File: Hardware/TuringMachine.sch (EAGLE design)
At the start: 83 parts, among them IC1 TL072P, IC2 4015, IC3 4015, IC5 4016, IC6 TL072P, IC7 TL072P, T1 2N3904, T2 2N3904, T3 2N3904

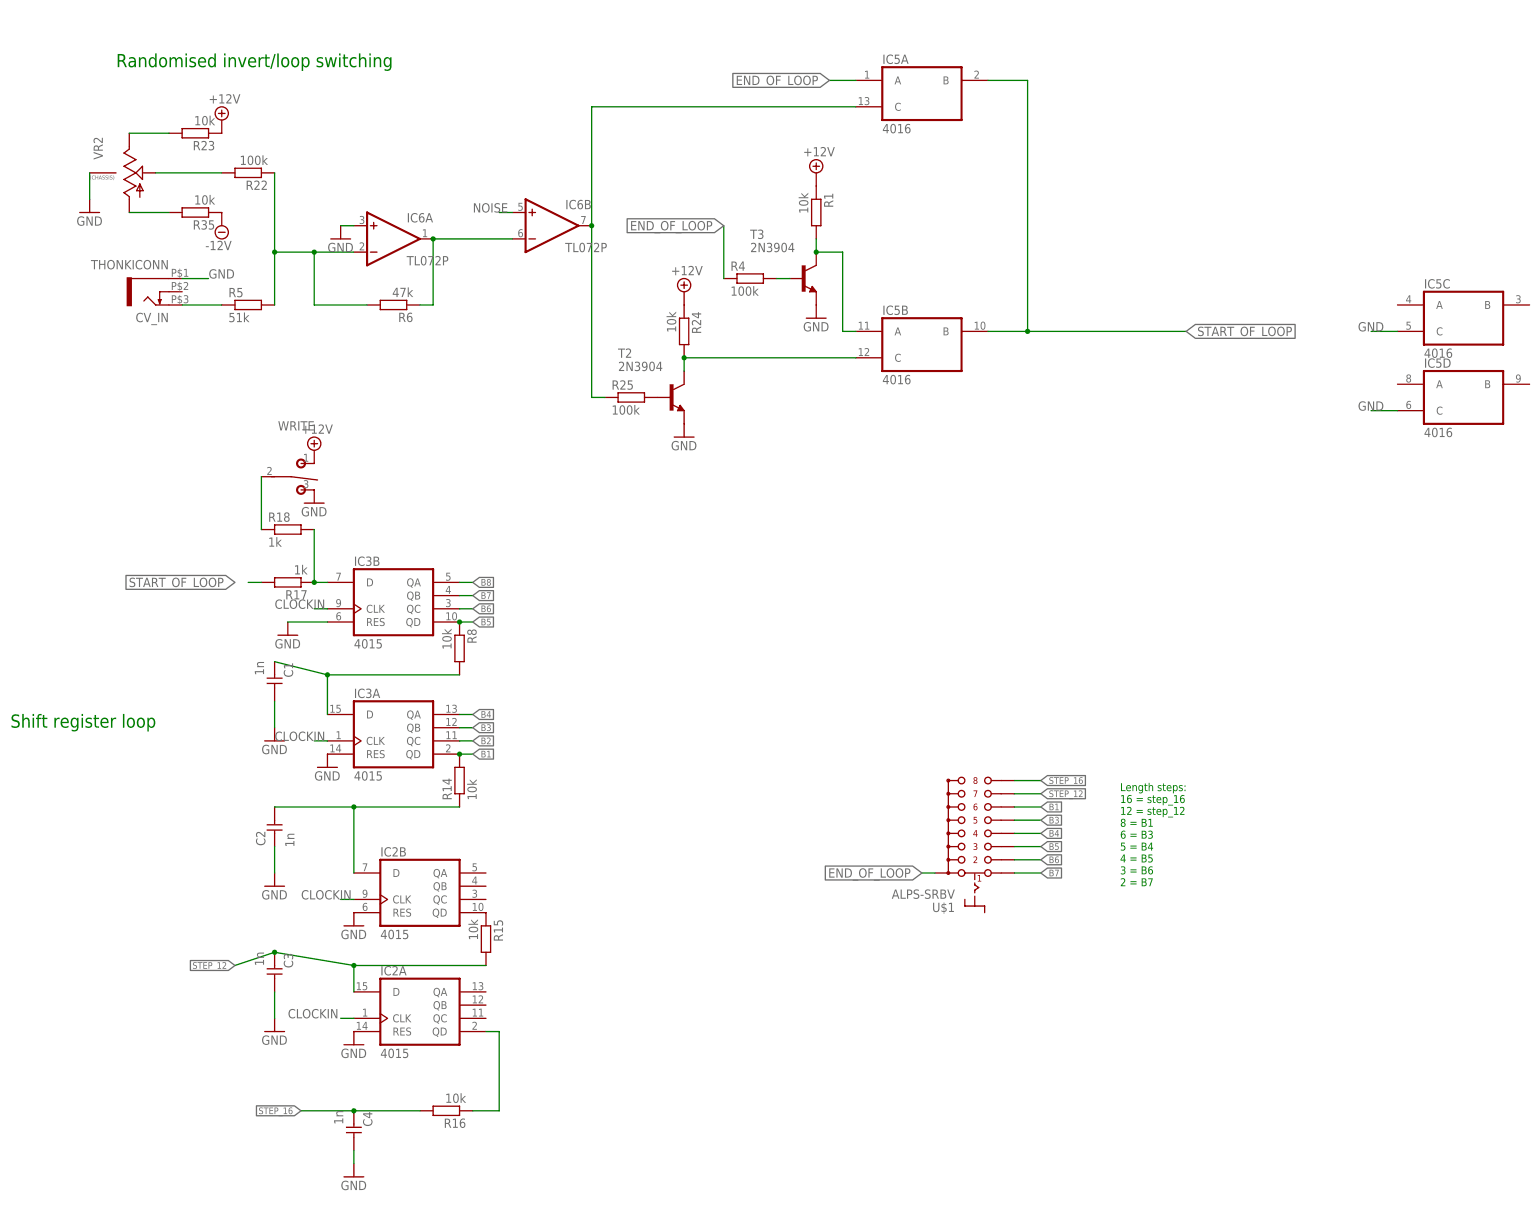
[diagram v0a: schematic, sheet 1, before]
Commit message: Move R16 & C4 to start of loop
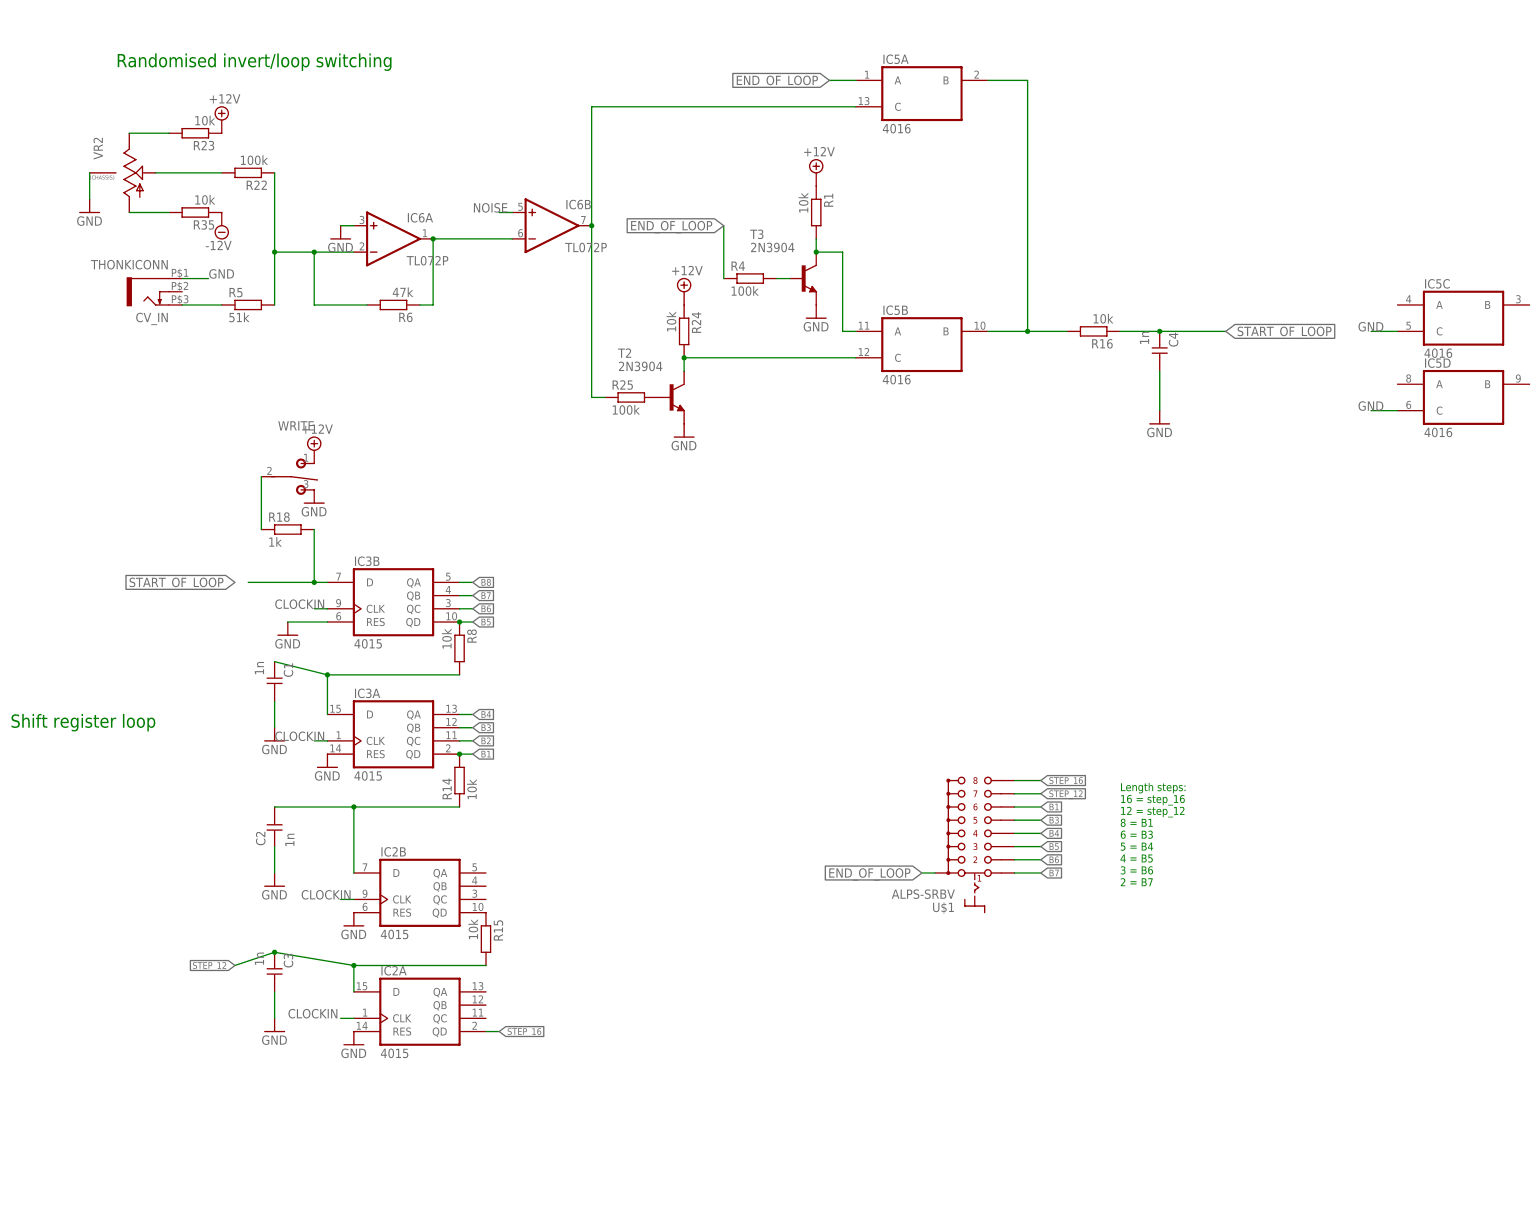
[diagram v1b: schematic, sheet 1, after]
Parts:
- removed R17: 1k, TomW:R-EU_0207/7
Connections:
- removed net N$19: IC3B.D, R17.1, R18.2
- removed net N$29: IC2A.QD, R16.1
- net START_OF_LOOP: now also C4.2, IC3B.D, R16.1, R16.2, R18.2; no longer R17.2
- net STEP_16: now also IC2A.QD; no longer C4.2, R16.2
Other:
- moved on the sheet: C4, R16
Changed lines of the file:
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@@
 <part name="GND6" library="supply1" deviceset="GND" device=""/>
 <part name="WRITE" library="TomW" deviceset="T-80-T-SPDT-ON-OFF-ON" device=""/>
-<part name="R17" library="TomW" deviceset="R-EU_" device="0207/7" value="1k"/>
 <part name="R18" library="TomW" deviceset="R-EU_" device="0207/7" value="1k"/>
 <part name="P+4" library="supply2" deviceset="+12V" device=""/>
@@
 <instance part="R14" gate="G$1" x="104.14" y="27.94" rot="R90"/>
 <instance part="R15" gate="G$1" x="109.22" y="-2.54" rot="R270"/>
-<instance part="R16" gate="G$1" x="101.6" y="-35.56" rot="R180"/>
-<instance part="C4" gate="G$1" x="83.82" y="-40.64" rot="R180"/>
+<instance part="R16" gate="G$1" x="226.06" y="114.3" rot="R180"/>
+<instance part="C4" gate="G$1" x="238.76" y="109.22" rot="R180"/>
 <instance part="GND4" gate="1" x="71.12" y="55.88"/>
 <instance part="GND14" gate="1" x="83.82" y="-22.86"/>
 <instance part="GND13" gate="1" x="83.82" y="0"/>
-<instance part="GND12" gate="1" x="83.82" y="-48.26"/>
+<instance part="GND12" gate="1" x="238.76" y="96.52"/>
 <instance part="GND7" gate="1" x="78.74" y="30.48"/>
 <instance part="GND8" gate="1" x="68.58" y="35.56"/>
@@
 <instance part="FRAME1" gate="G$2" x="236.22" y="-78.74"/>
 <instance part="WRITE" gate="G$1" x="71.12" y="88.9" rot="R270"/>
-<instance part="R17" gate="G$1" x="71.12" y="66.04" rot="R180"/>
 <instance part="R18" gate="G$1" x="71.12" y="76.2"/>
 <instance part="P+4" gate="+12V" x="76.2" y="91.44"/>
@@
 <net name="STEP_16" class="0">
 <segment>
-<pinref part="R16" gate="G$1" pin="2"/>
-<wire x1="96.52" y1="-35.56" x2="83.82" y2="-35.56" width="0.1524" layer="91"/>
-<pinref part="C4" gate="G$1" pin="2"/>
-<wire x1="73.66" y1="-35.56" x2="83.82" y2="-35.56" width="0.1524" layer="91"/>
-<junction x="83.82" y="-35.56"/>
-<label x="73.66" y="-35.56" size="1.27" layer="95" rot="R180" xref="yes"/>
-</segment>
-<segment>
 <pinref part="U$1" gate="G$1" pin="8"/>
 <wire x1="215.9" y1="27.94" x2="210.82" y2="27.94" width="0.1524" layer="91"/>
 <label x="215.9" y="27.94" size="1.27" layer="95" xref="yes"/>
 </segment>
-</net>
-<net name="N$19" class="0">
-<segment>
-<pinref part="IC3" gate="B" pin="D"/>
-<pinref part="R17" gate="G$1" pin="1"/>
-<wire x1="76.2" y1="66.04" x2="78.74" y2="66.04" width="0.1524" layer="91"/>
-<pinref part="R18" gate="G$1" pin="2"/>
-<wire x1="76.2" y1="76.2" x2="76.2" y2="66.04" width="0.1524" layer="91"/>
-<junction x="76.2" y="66.04"/>
+<segment>
+<pinref part="IC2" gate="A" pin="QD"/>
+<wire x1="111.76" y1="-20.32" x2="109.22" y2="-20.32" width="0.1524" layer="91"/>
+<label x="111.76" y="-20.32" size="1.27" layer="95" xref="yes"/>
 </segment>
 </net>
@@
 <pinref part="C4" gate="G$1" pin="1"/>
 <pinref part="GND12" gate="1" pin="GND"/>
-<wire x1="83.82" y1="-45.72" x2="83.82" y2="-43.18" width="0.1524" layer="91"/>
+<wire x1="238.76" y1="99.06" x2="238.76" y2="106.68" width="0.1524" layer="91"/>
 </segment>
 <segment>
@@
 <net name="START_OF_LOOP" class="0">
 <segment>
-<wire x1="66.04" y1="66.04" x2="63.5" y2="66.04" width="0.1524" layer="91"/>
-<pinref part="R17" gate="G$1" pin="2"/>
 <label x="60.96" y="66.04" size="1.778" layer="95" rot="R180" xref="yes"/>
+<pinref part="IC3" gate="B" pin="D"/>
+<wire x1="76.2" y1="66.04" x2="78.74" y2="66.04" width="0.1524" layer="91"/>
+<pinref part="R18" gate="G$1" pin="2"/>
+<wire x1="76.2" y1="76.2" x2="76.2" y2="66.04" width="0.1524" layer="91"/>
+<wire x1="63.5" y1="66.04" x2="76.2" y2="66.04" width="0.1524" layer="91"/>
+<junction x="76.2" y="66.04"/>
 </segment>
 <segment>
 <pinref part="IC5" gate="B" pin="B"/>
 <wire x1="205.74" y1="114.3" x2="213.36" y2="114.3" width="0.1524" layer="91"/>
-<wire x1="213.36" y1="114.3" x2="243.84" y2="114.3" width="0.1524" layer="91"/>
-<label x="243.84" y="114.3" size="1.778" layer="95" xref="yes"/>
 <pinref part="IC5" gate="A" pin="B"/>
 <wire x1="205.74" y1="162.56" x2="213.36" y2="162.56" width="0.1524" layer="91"/>
 <wire x1="213.36" y1="162.56" x2="213.36" y2="114.3" width="0.1524" layer="91"/>
+<pinref part="R16" gate="G$1" pin="2"/>
+<wire x1="220.98" y1="114.3" x2="213.36" y2="114.3" width="0.1524" layer="91"/>
 <junction x="213.36" y="114.3"/>
+</segment>
+<segment>
+<pinref part="R16" gate="G$1" pin="1"/>
+<pinref part="C4" gate="G$1" pin="2"/>
+<wire x1="231.14" y1="114.3" x2="238.76" y2="114.3" width="0.1524" layer="91"/>
+<wire x1="238.76" y1="114.3" x2="251.46" y2="114.3" width="0.1524" layer="91"/>
+<junction x="238.76" y="114.3"/>
+<label x="251.46" y="114.3" size="1.778" layer="95" xref="yes"/>
 </segment>
 </net>
@@
 </segment>
 </net>
-<net name="N$29" class="0">
-<segment>
-<pinref part="R16" gate="G$1" pin="1"/>
-<wire x1="106.68" y1="-35.56" x2="111.76" y2="-35.56" width="0.1524" layer="91"/>
-<wire x1="111.76" y1="-35.56" x2="111.76" y2="-20.32" width="0.1524" layer="91"/>
-<pinref part="IC2" gate="A" pin="QD"/>
-<wire x1="111.76" y1="-20.32" x2="109.22" y2="-20.32" width="0.1524" layer="91"/>
-</segment>
-</net>
